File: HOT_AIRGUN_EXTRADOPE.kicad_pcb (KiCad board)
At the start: 2 copper layers, 99 parts, among them J5 Conn_01x04_Socket, J6 Conn_01x05_Pin, J7 Conn_01x02_Socket, J8 Conn_02x05_Counter_Clockwise, J9 Conn_02x03_Counter_Clockwise, Q3 BT136-500, Q4 BT136-500, Q5 S9013_C402281, Q6 S9013_C402281, Q7 AO3400_C2938367, Q8 AO3400_C2938367, Q9 AO3400_C2938367, SW1 TSB008A2526A, SW2 TSB008A2526A, T1 MOC3020M, T2 MOC3020M, U1 EL817S1C(F), U10 DB301V-3.5-2P-GN, U11 DB301V-3.5-2P-GN, U12 DB301V-3.5-2P-GN, U13 DB301V-3.5-2P-GN, U14 DB301V-3.5-2P-GN, U15 DB301V-3.5-2P-GN, U2 ESP32-WROOM-32D, U3 TL431BIDBZR, U4 TL431ACDR, U5 XL1509-5.0E1, U6 RS321BXF, U7 AMS1117-3.3, U8 RS321BXF, U9 DB301V-3.5-2P-GN

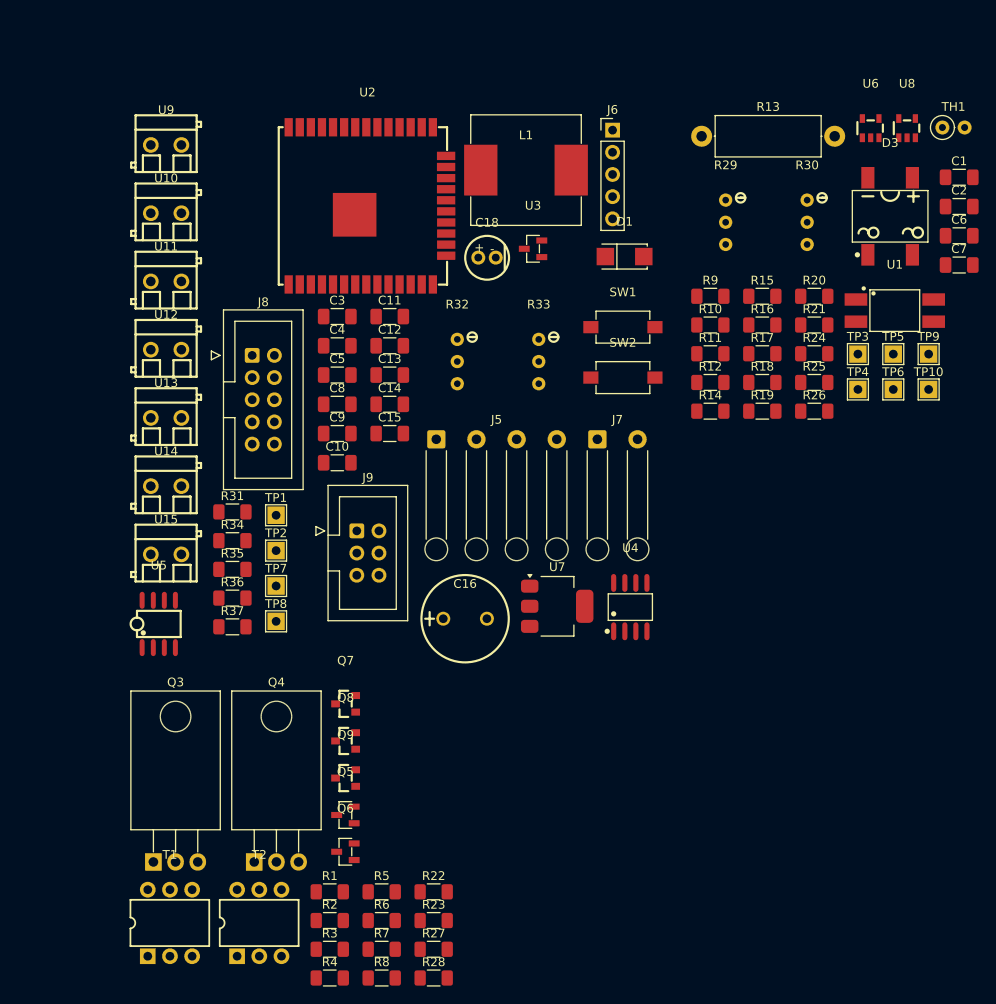
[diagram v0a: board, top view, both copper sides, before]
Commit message: Finished Routing, Finished Schematic
Yet to add , solderMask
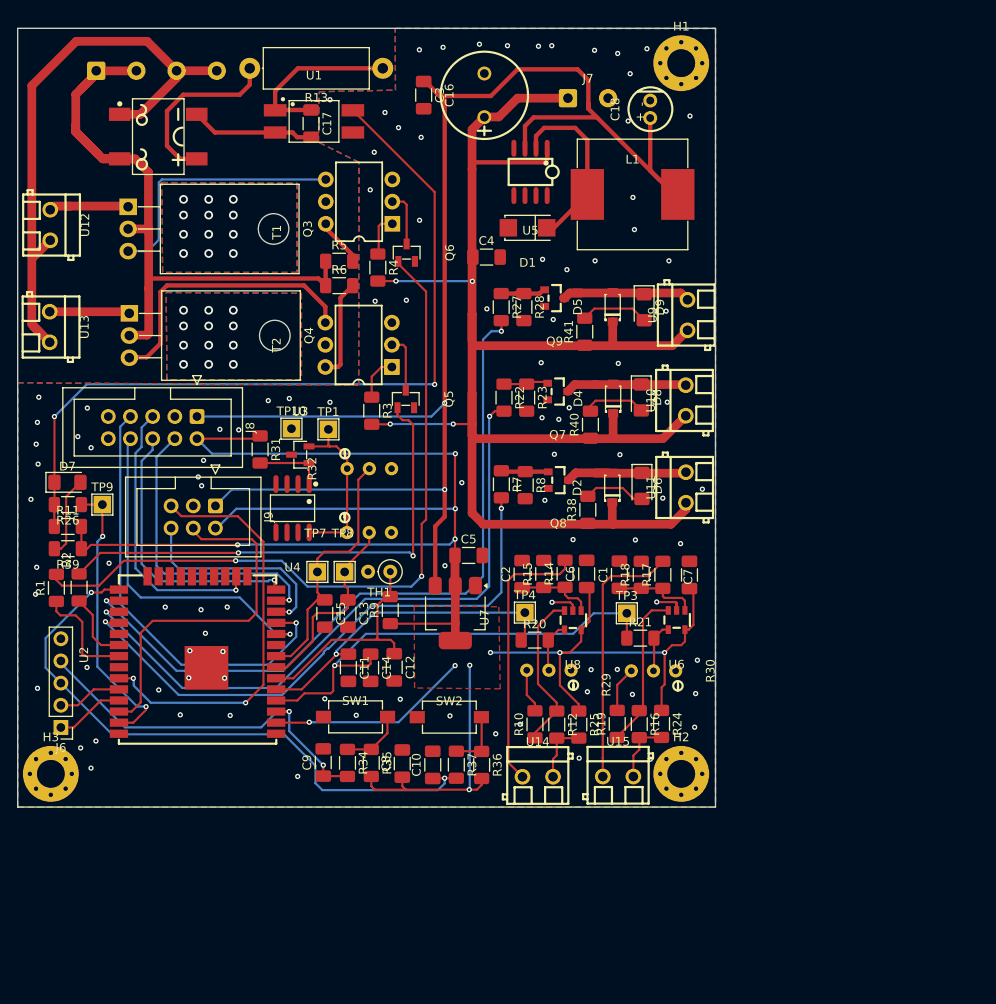
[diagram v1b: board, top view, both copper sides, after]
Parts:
- removed TP2: Vref_TPgnd, TestPoint:TestPoint_THTPad_2.0x2.0mm_Drill1.0mm
- removed TP5, TP6: TC1_TPgnd, TestPoint:TestPoint_THTPad_2.0x2.0mm_Drill1.0mm
- added C17: 100nF, Capacitor_SMD:C_1206_3216Metric_Pad1.33x1.80mm_HandSolder, F.Cu at (50.0, 26.2)
- added D2: SD103AW_C181204, EasyEDA:SOD-123_L2.8-W1.8-LS3.7-RD, F.Cu at (84.5, 67.9)
- added D4: SD103AW_C181204, EasyEDA:SOD-123_L2.8-W1.8-LS3.7-RD, F.Cu at (84.6, 57.7)
- added D5: SD103AW_C181204, EasyEDA:SOD-123_L2.8-W1.8-LS3.7-RD, F.Cu at (84.6, 47.2)
- added D6: LED, LED_SMD:LED_1206_3216Metric_Pad1.42x1.75mm_HandSolder, F.Cu at (87.9, 67.7)
- added D7: LED, LED_SMD:LED_1206_3216Metric_Pad1.42x1.75mm_HandSolder, F.Cu at (22.1, 67.3)
- added D8: LED, LED_SMD:LED_1206_3216Metric_Pad1.42x1.75mm_HandSolder, F.Cu at (87.9, 57.6)
- added D9: LED, LED_SMD:LED_1206_3216Metric_Pad1.42x1.75mm_HandSolder, F.Cu at (88.2, 47.2)
- added H1: MountingHole, MountingHole:MountingHole_3.2mm_M3_Pad_Via, F.Cu at (92.4, 19.3)
- added H2: MountingHole, MountingHole:MountingHole_3.2mm_M3_Pad_Via, F.Cu at (92.4, 100.7)
- added H3: MountingHole, MountingHole:MountingHole_3.2mm_M3_Pad_Via, F.Cu at (20.2, 100.7)
- added R38: 10k, Resistor_SMD:R_1206_3216Metric_Pad1.30x1.75mm_HandSolder, F.Cu at (81.7, 70.4)
- added R39: 1k, Resistor_SMD:R_1206_3216Metric_Pad1.30x1.75mm_HandSolder, F.Cu at (22.2, 74.9)
- added R40: 10k, Resistor_SMD:R_1206_3216Metric_Pad1.30x1.75mm_HandSolder, F.Cu at (82.0, 60.7)
- added R41: 10k, Resistor_SMD:R_1206_3216Metric_Pad1.30x1.75mm_HandSolder, F.Cu at (81.4, 50.0)
- C11, C12, C13, C14, C15: value 1u -> 100n
- J5: footprint Connector_Wire:SolderWire-0.5sqmm_1x04_P4.6mm_D0.9mm_OD2.1mm_Relief -> Connector_Wire:SolderWire-0.5sqmm_1x04_P4.6mm_D0.9mm_OD2.1mm; moved to B.Cu
- J7: footprint Connector_Wire:SolderWire-0.5sqmm_1x02_P4.6mm_D0.9mm_OD2.1mm_Relief -> Connector_Wire:SolderWire-0.5sqmm_1x02_P4.6mm_D0.9mm_OD2.1mm
- TP10: value ZCS_TPgnd -> GND_TP
- moved TP9 96.2 mm to (26.1, 69.8)
- moved J6 93.1 mm to (21.4, 95.4), turned to 180 degrees
- moved R26 86.2 mm to (22.2, 69.8), turned to 180 degrees
- moved T1 85.4 mm to (55.5, 35.1), turned to 90 degrees
- moved D3 84.3 mm to (32.5, 27.7), turned to -90 degrees
- moved R4 81.6 mm to (57.7, 42.7), turned to -90 degrees
- moved TH1 81.2 mm to (59.1, 77.5), turned to 180 degrees
- moved R28 77.5 mm to (74.4, 47.2), turned to -90 degrees
- moved R11 76.2 mm to (22.2, 72.3)
- moved Q3 75.1 mm to (29.1, 35.7), turned to -90 degrees
- moved R27 74.0 mm to (71.8, 47.2), turned to -90 degrees
- moved TP10 73.1 mm to (47.8, 61.1)
- moved R6 72.9 mm to (53.3, 44.8)
- moved R5 72.4 mm to (53.3, 42.0)
- moved U1 70.0 mm to (50.4, 26.0)
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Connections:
- net AcLoad1- renamed NEUT
- net DC_Load1+ renamed +24V
- C6 pad 1: 3.3V -> +3.3V
- C7 pad 1: 3.3V -> +3.3V
- R11 pad 1: /ZCD -> Net-(D7-K)
- R12 pad 2: Termocouple1 - -> Termocouple1-
- R14 pad 2: Termocouple1 + -> Termocouple1+
- R16 pad 2: Termocouple2 - -> Termocouple2-
- R17 pad 2: Termocouple2 + -> Termocouple2+
- R24 pad 1: 3.3V -> +3.3V
- R24 pad 2: Termocouple2 - -> Termocouple2-
- R25 pad 1: 3.3V -> +3.3V
- R25 pad 2: Termocouple1 - -> Termocouple1-
- R26 pad 2: Net-(R26-Pad2) -> Net-(D7-K)
- R29 pad 1: Net-(R10-Pad2) -> unconnected-(R29-Pad1)
- R29 pad 3: unconnected-(R29-Pad3) -> Net-(R10-Pad2)
- R30 pad 1: Net-(R19-Pad2) -> unconnected-(R30-Pad1)
- R30 pad 3: unconnected-(R30-Pad3) -> Net-(R19-Pad2)
- R32 pad 1: /VREF_2p5 -> /VREF2p5
- R33 pad 1: /VREF_2p5 -> /VREF2p5
- U1 pad 4: Net-(R26-Pad2) -> Net-(D7-K)
- U2 pad 4: /VREFAtt1 -> ThermocoupleSig2
- U2 pad 5: /VREFAtt2 -> ThermocoupleSig1
- U2 pad 7: ThermocoupleSig1 -> /VREFAtt2
- U2 pad 8: ThermocoupleSig2 -> /VREFAtt1
- U4 pad 8: /VREF_2p5 -> /VREF2p5
- U6 pad 5: 3.3V -> +3.3V
- U8 pad 5: 3.3V -> +3.3V
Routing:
- net +3.3V: track 0.00 -> 248.3 mm, vias 0 -> 11
- net +24V: track 0.00 -> 182.9 mm, vias 0 -> 4
- net +5V: track 0.00 -> 171.6 mm, vias 0 -> 2
- net Net-(D7-K): track 0.00 -> 94.6 mm, vias 0 -> 2
- net Net-(Q6-B): track 0.00 -> 83.7 mm, vias 0 -> 2
- net DcControl3: track 0.00 -> 83.2 mm, vias 0 -> 2
- net LINE: track 0.00 -> 80.2 mm
- net DcControl2: track 0.00 -> 75.1 mm, vias 0 -> 2
- net /BOOT_MODE: track 0.00 -> 70.5 mm, vias 0 -> 2
- net NEUT: track 0.00 -> 68.9 mm
- net DcControl1: track 0.00 -> 66.2 mm, vias 0 -> 2
- net Net-(Q5-B): track 0.00 -> 57.5 mm, vias 0 -> 2
- net ThermocoupleSig2: track 0.00 -> 54.0 mm, vias 0 -> 1
- net /SPI_CS0: track 0.00 -> 50.2 mm, vias 0 -> 1
- net /I2C_SDA: track 0.00 -> 47.7 mm, vias 0 -> 2
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- added copper zone on F.Cu, net +3.3V
- added copper zone on B.Cu, net GND
- added copper zone on F.Cu, net GND
- added copper zone on B.Cu, net Triac1_Heatpad
- added copper zone on F.Cu, net Triac1_Heatpad
- added copper zone on B.Cu, net Triac2_Heatpad
- added copper zone on F.Cu, net Triac2_Heatpad
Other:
- board outline added: 79.9 x 89.2 mm
